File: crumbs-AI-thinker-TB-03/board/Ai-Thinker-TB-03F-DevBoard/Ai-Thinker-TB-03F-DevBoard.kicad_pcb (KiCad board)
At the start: 2 copper layers, 50 x 25 mm, 30 parts, among them J1 L_Conn, J2 R_Conn, P1 USB_C_Plug_USB2.0, SW1 RST, SW2 DTR, U1 CH340C, U2 AI_Thinker_TB-03F, U3 AMS1117-3.3

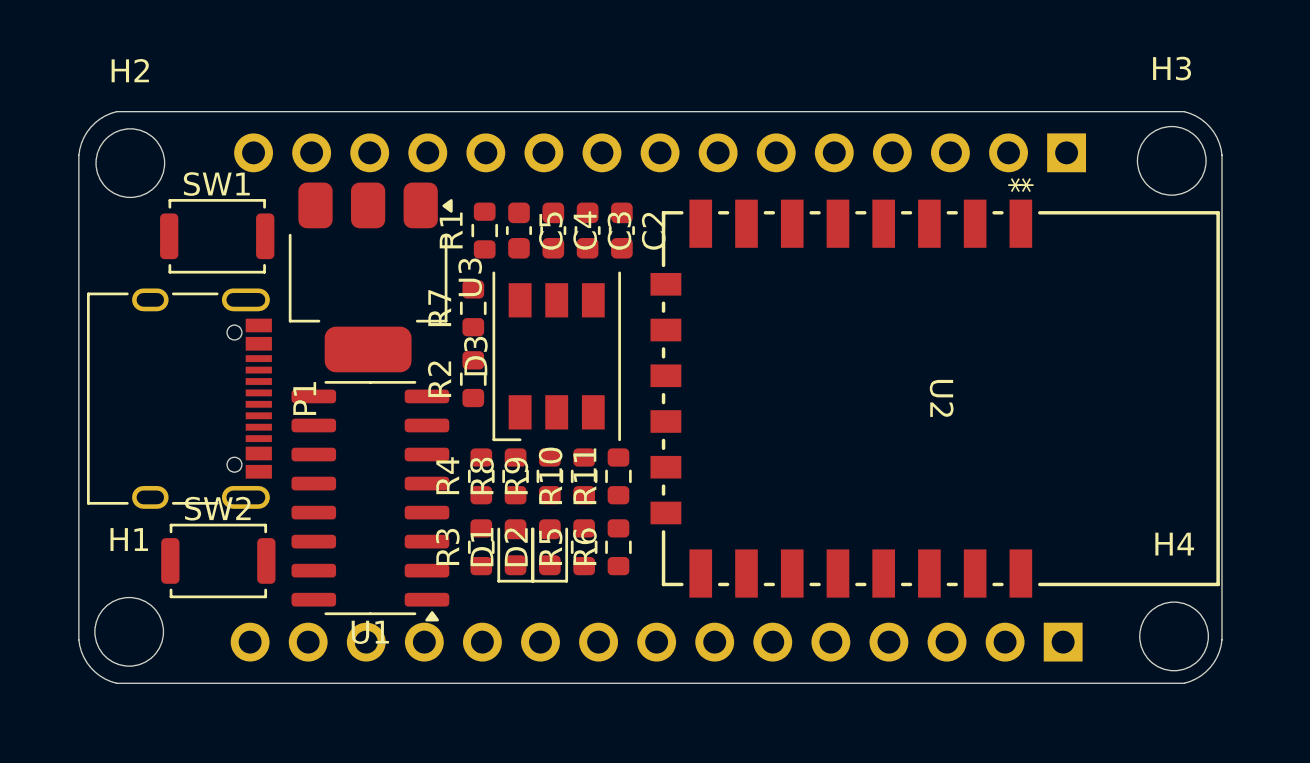
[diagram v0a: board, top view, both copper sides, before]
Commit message: [12-11-2017] TB-03 Finish Routing, Need Recheck Board and Schematic
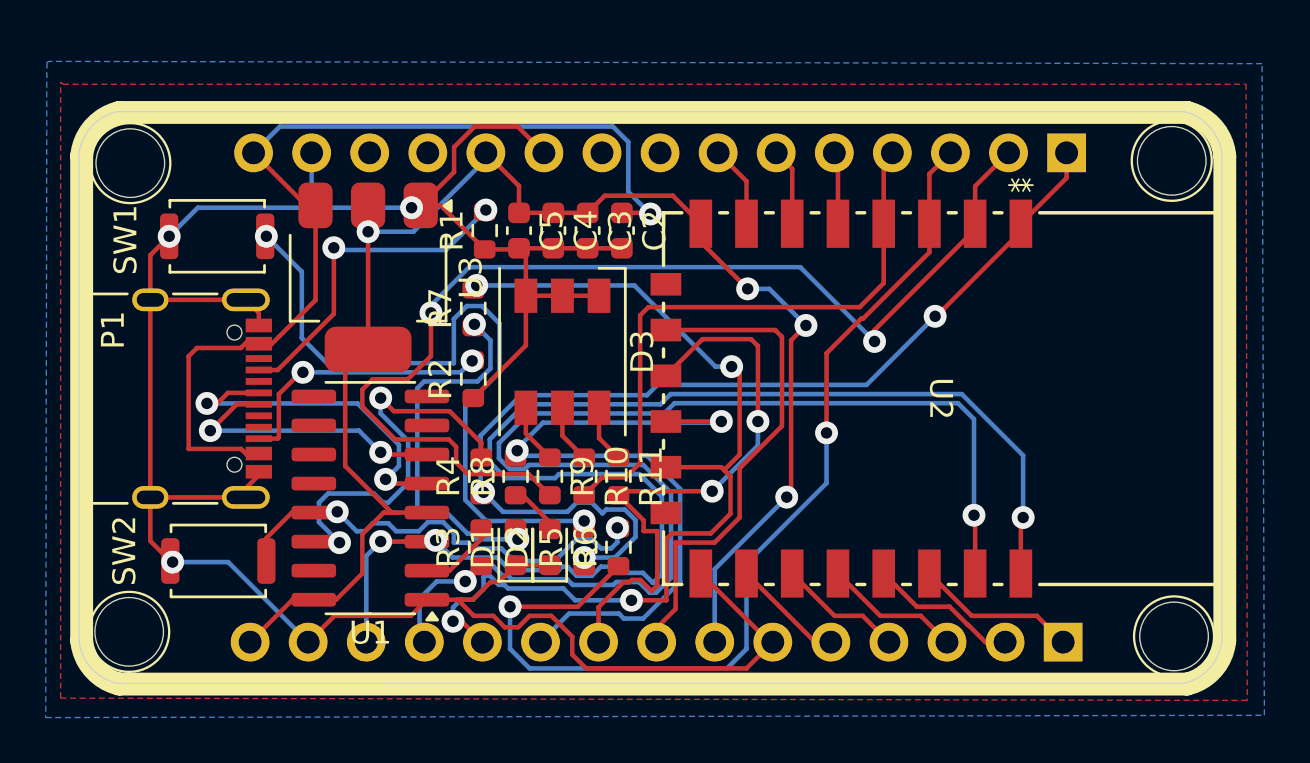
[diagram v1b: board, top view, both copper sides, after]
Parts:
- moved D3 0.32 mm to (91.8, 60.6), turned to -90 degrees
- turned R10 to -90 degrees
- turned R11 to -90 degrees
- turned R9 to -90 degrees
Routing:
- net GND: track 0.00 -> 108.6 mm, vias 0 -> 3
- net +3V3: track 0.00 -> 67.1 mm, vias 0 -> 4
- net /RXD: track 0.00 -> 61.5 mm, vias 0 -> 3
- net /TXD: track 0.00 -> 56.7 mm, vias 0 -> 2
- net /PC4: track 0.00 -> 48.9 mm, vias 0 -> 2
- net /RST: track 0.00 -> 46.1 mm, vias 0 -> 3
- net /SWS: track 0.00 -> 43.8 mm, vias 0 -> 2
- net +5V: track 0.00 -> 43.3 mm, vias 0 -> 1
- net /PB5: track 0.00 -> 41.3 mm, vias 0 -> 4
- net /PB4: track 0.00 -> 31.5 mm, vias 0 -> 2
- net Net-(R5-Pad2): track 0.00 -> 31.0 mm, vias 0 -> 2
- net /PC3: track 0.00 -> 26.6 mm
- net /PC2: track 0.00 -> 26.1 mm, vias 0 -> 2
- net /PA1: track 0.00 -> 21.8 mm
- net /DTR: track 0.00 -> 20.0 mm, vias 0 -> 2
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- added copper zone on F.Cu, net +3V3
- added copper zone on B.Cu, net GND
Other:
- board text added: "Crumbs Series AI Thinker TB-03F"

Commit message: [12-12-2151] create logo and arrange silkscreen
Update README.md
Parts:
- added G12: LOGO, library:Crumbs-Logo_Footprint_13x13, F.Cu at (108.2, 62.1)
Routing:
- net +3V3: track 67.1 -> 71.6 mm
- net /PB5: track 41.3 -> 38.9 mm
- net /PC2: track 26.1 -> 23.8 mm
- net /TXD: track 56.7 -> 54.8 mm
- net /RXD: track 61.5 -> 59.8 mm
- net /DTR: track 20.0 -> 18.7 mm
- net Net-(D1-A): track 16.6 -> 15.8 mm
- net GND: track 108.6 -> 109.3 mm
- net /RTS: track 17.9 -> 17.3 mm
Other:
- board text added: "3.3V"
- board text added: "5V"
- board text added: "A1"
- board text added: "B4"
- board text added: "B5"
- board text added: "B6"
- board text added: "B7"
- board text added: "C0"
- board text added: "C1"
- board text added: "C2"
- board text added: "C3"
- board text added: "C4"
- board text added: "D2"
- board text added: "D3"
- board text added: "D4"
- board text added: "D7"
- board text added: "GND"
- board text added: "RST"
- board text added: "RXD"
- board text added: "SWS"
- board text added: "TXD"
- board text added: "X"

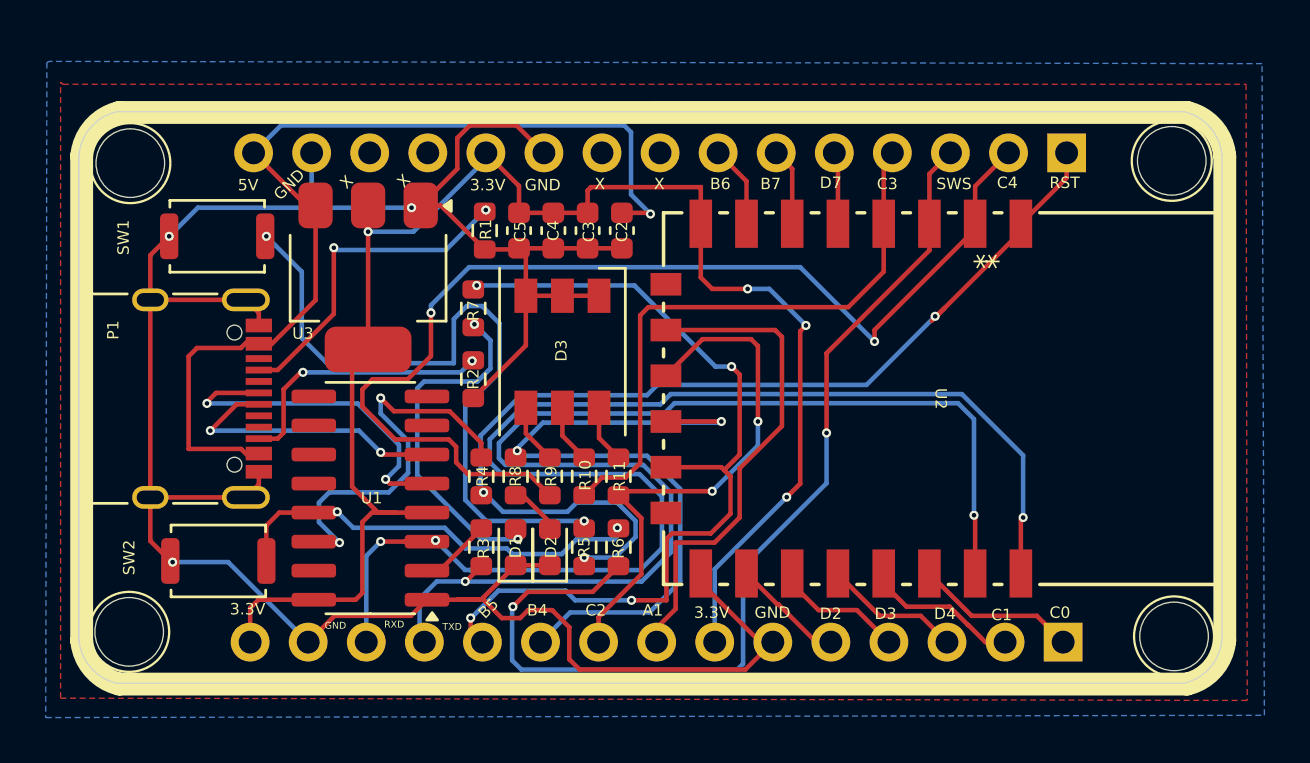
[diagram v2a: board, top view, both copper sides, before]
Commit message: [01-15-1749] add black magic probe to crumbs
add black magic probe

nit document

update schematic
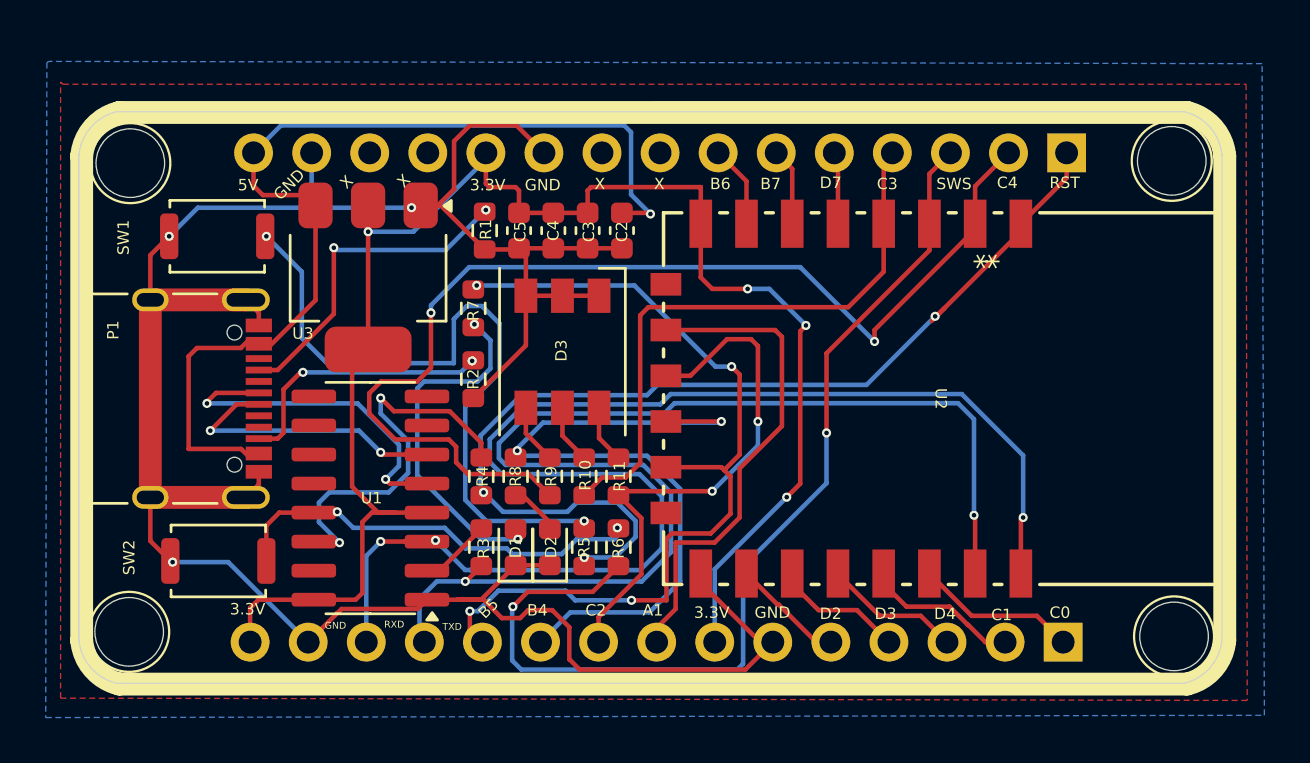
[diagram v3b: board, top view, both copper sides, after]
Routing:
- net +5V: track 43.7 -> 44.5 mm
- net +3V3: track 71.6 -> 72.3 mm
